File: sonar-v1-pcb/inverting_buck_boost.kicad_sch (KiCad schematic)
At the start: 0 parts

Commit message: wip
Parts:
- added U4: AP63301WU-7, Sonar:TSOT-23-6, symbol sonar_lib:AP63301WU-7
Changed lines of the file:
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@@
 	(generator_version "9.0")
 	(paper "A4")
+	(symbol
+		(lib_id "sonar_lib:AP63301WU-7")
+		(at 148.59 93.98 0)
+		(unit 1)
+		(exclude_from_sim no)
+		(in_bom yes)
+		(on_board yes)
+		(dnp no)
+		(fields_autoplaced yes)
+		(property "Reference" "U4"
+			(at 148.59 78.74 0)
+			(effects
+				(font
+					(size 1.27 1.27)
+				)
+			)
+		)
+		(property "Value" "AP63301WU-7"
+			(at 148.59 81.28 0)
+			(effects
+				(font
+					(size 1.27 1.27)
+				)
+			)
+		)
+		(property "Footprint" "Sonar:TSOT-23-6"
+			(at 148.59 63.5 0)
+			(effects
+				(font
+					(size 1.27 1.27)
+				)
+				(hide yes)
+			)
+		)
+		(property "Datasheet" "https://www.lcsc.com/datasheet/C2158003.pdf"
+			(at 148.59 76.2 0)
+			(effects
+				(font
+					(size 1.27 1.27)
+				)
+				(hide yes)
+			)
+		)
+		(property "Description" "500kHz Adjustable Buck Converter, 3A Max Current, 3.8V-32V Input Voltage"
+			(at 148.59 73.66 0)
+			(effects
+				(font
+					(size 1.27 1.27)
+				)
+				(hide yes)
+			)
+		)
+		(property "Manufacturer" "DIODES"
+			(at 148.59 58.42 0)
+			(effects
+				(font
+					(size 1.27 1.27)
+				)
+				(hide yes)
+			)
+		)
+		(property "Mfr. Part #" "AP63301WU-7"
+			(at 148.59 60.96 0)
+			(effects
+				(font
+					(size 1.27 1.27)
+				)
+				(hide yes)
+			)
+		)
+		(property "LCSC ID" "C2158003"
+			(at 148.59 71.12 0)
+			(effects
+				(font
+					(size 1.27 1.27)
+				)
+				(hide yes)
+			)
+		)
+		(property "Package" "TSOT-23-6"
+			(at 148.59 68.58 0)
+			(effects
+				(font
+					(size 1.27 1.27)
+				)
+				(hide yes)
+			)
+		)
+		(property "Spice Warning Override" "No SPICE model available"
+			(at 148.59 66.04 0)
+			(effects
+				(font
+					(size 1.27 1.27)
+				)
+				(hide yes)
+			)
+		)
+		(pin "4"
+		)
+		(pin "2"
+		)
+		(pin "1"
+		)
+		(pin "5"
+		)
+		(pin "6"
+		)
+		(pin "3"
+		)
+		(instances
+			(project ""
+				(path "/f72ceae0-eee4-4385-b0e8-639846bcb5f2/0971c334-b681-41ae-ad35-a89520df0687/b540816d-de86-42bd-acdb-d7039b5ee686"
+					(reference "U4")
+					(unit 1)
+				)
+			)
+		)
+	)
 )

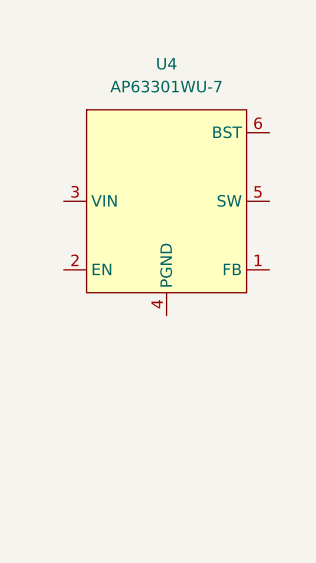
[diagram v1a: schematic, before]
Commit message: Add a buck converter for the inverting buck boost
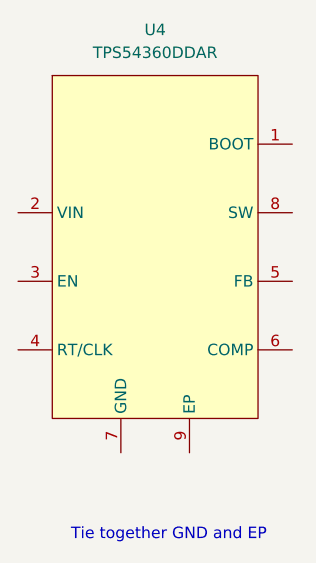
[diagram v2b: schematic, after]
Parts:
- removed U4: AP63301WU-7, Sonar:TSOT-23-6, symbol sonar_lib:AP63301WU-7
- added U4: TPS54360DDAR, GS_SO:SOIC-8-1EP_3.9x4.9mm_P1.27mm_EP2.29x3mm, symbol GS_Switching_Regulators:TPS54360DDAR
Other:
- note added: "Tie together GND and EP"
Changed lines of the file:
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@@
 	(generator_version "9.0")
 	(paper "A4")
+	(text "Tie together GND and EP"
+		(exclude_from_sim no)
+		(at 148.844 131.064 0)
+		(effects
+			(font
+				(size 1.27 1.27)
+			)
+		)
+	)
 	(symbol
-		(lib_id "sonar_lib:AP63301WU-7")
-		(at 148.59 93.98 0)
+		(lib_id "GS_Switching_Regulators:TPS54360DDAR")
+		(at 147.32 99.06 0)
 		(unit 1)
 		(exclude_from_sim no)
@@
 		(fields_autoplaced yes)
 		(property "Reference" "U4"
-			(at 148.59 78.74 0)
+			(at 147.32 74.93 0)
 			(effects
 				(font
@@
 			)
 		)
-		(property "Value" "AP63301WU-7"
-			(at 148.59 81.28 0)
+		(property "Value" "TPS54360DDAR"
+			(at 147.32 77.47 0)
 			(effects
 				(font
@@
 			)
 		)
-		(property "Footprint" "Sonar:TSOT-23-6"
-			(at 148.59 63.5 0)
+		(property "Footprint" "GS_SO:SOIC-8-1EP_3.9x4.9mm_P1.27mm_EP2.29x3mm"
+			(at 147.32 66.04 0)
 			(effects
 				(font
@@
 			)
 		)
-		(property "Datasheet" "https://www.lcsc.com/datasheet/C2158003.pdf"
-			(at 148.59 76.2 0)
+		(property "Datasheet" "https://www.lcsc.com/datasheet/C44377.pdf"
+			(at 147.32 58.42 0)
 			(effects
 				(font
@@
 			)
 		)
-		(property "Description" "500kHz Adjustable Buck Converter, 3A Max Current, 3.8V-32V Input Voltage"
-			(at 148.59 73.66 0)
+		(property "Description" "2.5MHz Adjustable Buck Converter, 4.5V-60V Input Voltage, 3.5A Max Current"
+			(at 147.32 68.58 0)
 			(effects
 				(font
@@
 			)
 		)
-		(property "Manufacturer" "DIODES"
-			(at 148.59 58.42 0)
+		(property "Manufacturer" "TI"
+			(at 147.32 73.66 0)
 			(effects
 				(font
@@
 			)
 		)
-		(property "Mfr. Part #" "AP63301WU-7"
-			(at 148.59 60.96 0)
+		(property "Mfr. Part #" "TPS54360DDAR"
+			(at 147.32 60.96 0)
 			(effects
 				(font
@@
 			)
 		)
-		(property "LCSC ID" "C2158003"
-			(at 148.59 71.12 0)
+		(property "LCSC ID" "C44377"
+			(at 147.32 63.5 0)
 			(effects
 				(font
@@
 			)
 		)
-		(property "Package" "TSOT-23-6"
-			(at 148.59 68.58 0)
+		(property "Package" "SOIC-8-EP"
+			(at 147.32 71.12 0)
 			(effects
 				(font
@@
 			)
 		)
-		(property "Spice Warning Override" "No SPICE model available"
-			(at 148.59 66.04 0)
-			(effects
-				(font
-					(size 1.27 1.27)
-				)
-				(hide yes)
-			)
+		(pin "5"
 		)
 		(pin "4"
 		)
-		(pin "2"
+		(pin "7"
+		)
+		(pin "9"
+		)
+		(pin "3"
+		)
+		(pin "8"
 		)
 		(pin "1"
 		)
-		(pin "5"
+		(pin "2"
 		)
 		(pin "6"
 		)
-		(pin "3"
-		)
 		(instances

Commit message: formatting lol
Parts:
- removed U4: TPS54360DDAR, GS_SO:SOIC-8-1EP_3.9x4.9mm_P1.27mm_EP2.29x3mm, symbol GS_Switching_Regulators:TPS54360DDAR
- added U4: AP63301WU-7, Sonar:TSOT-23-6, symbol sonar_lib:AP63301WU-7
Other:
- note removed: "Tie together GND and EP"
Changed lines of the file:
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@@
 	(generator_version "9.0")
 	(paper "A4")
-	(text "Tie together GND and EP"
-		(exclude_from_sim no)
-		(at 148.844 131.064 0)
-		(effects
-			(font
-				(size 1.27 1.27)
-			)
-		)
-	)
 	(symbol
-		(lib_id "GS_Switching_Regulators:TPS54360DDAR")
-		(at 147.32 99.06 0)
+		(lib_id "sonar_lib:AP63301WU-7")
+		(at 148.59 93.98 0)
 		(unit 1)
 		(exclude_from_sim no)
@@
 		(fields_autoplaced yes)
 		(property "Reference" "U4"
-			(at 147.32 74.93 0)
+			(at 148.59 78.74 0)
 			(effects
 				(font
@@
 			)
 		)
-		(property "Value" "TPS54360DDAR"
-			(at 147.32 77.47 0)
+		(property "Value" "AP63301WU-7"
+			(at 148.59 81.28 0)
 			(effects
 				(font
@@
 			)
 		)
-		(property "Footprint" "GS_SO:SOIC-8-1EP_3.9x4.9mm_P1.27mm_EP2.29x3mm"
-			(at 147.32 66.04 0)
+		(property "Footprint" "Sonar:TSOT-23-6"
+			(at 148.59 63.5 0)
 			(effects
 				(font
@@
 			)
 		)
-		(property "Datasheet" "https://www.lcsc.com/datasheet/C44377.pdf"
-			(at 147.32 58.42 0)
+		(property "Datasheet" "https://www.lcsc.com/datasheet/C2158003.pdf"
+			(at 148.59 76.2 0)
 			(effects
 				(font
@@
 			)
 		)
-		(property "Description" "2.5MHz Adjustable Buck Converter, 4.5V-60V Input Voltage, 3.5A Max Current"
-			(at 147.32 68.58 0)
+		(property "Description" "500kHz Adjustable Buck Converter, 3A Max Current, 3.8V-32V Input Voltage"
+			(at 148.59 73.66 0)
 			(effects
 				(font
@@
 			)
 		)
-		(property "Manufacturer" "TI"
-			(at 147.32 73.66 0)
+		(property "Manufacturer" "DIODES"
+			(at 148.59 58.42 0)
 			(effects
 				(font
@@
 			)
 		)
-		(property "Mfr. Part #" "TPS54360DDAR"
-			(at 147.32 60.96 0)
+		(property "Mfr. Part #" "AP63301WU-7"
+			(at 148.59 60.96 0)
 			(effects
 				(font
@@
 			)
 		)
-		(property "LCSC ID" "C44377"
-			(at 147.32 63.5 0)
+		(property "LCSC ID" "C2158003"
+			(at 148.59 71.12 0)
 			(effects
 				(font
@@
 			)
 		)
-		(property "Package" "SOIC-8-EP"
-			(at 147.32 71.12 0)
+		(property "Package" "TSOT-23-6"
+			(at 148.59 68.58 0)
 			(effects
 				(font
@@
 			)
 		)
-		(pin "5"
+		(property "Spice Warning Override" "No SPICE model available"
+			(at 148.59 66.04 0)
+			(effects
+				(font
+					(size 1.27 1.27)
+				)
+				(hide yes)
+			)
 		)
 		(pin "4"
 		)
-		(pin "7"
+		(pin "2"
 		)
-		(pin "9"
+		(pin "1"
+		)
+		(pin "5"
+		)
+		(pin "6"
 		)
 		(pin "3"
 		)
-		(pin "8"
-		)
-		(pin "1"
-		)
-		(pin "2"
-		)
-		(pin "6"
-		)
 		(instances

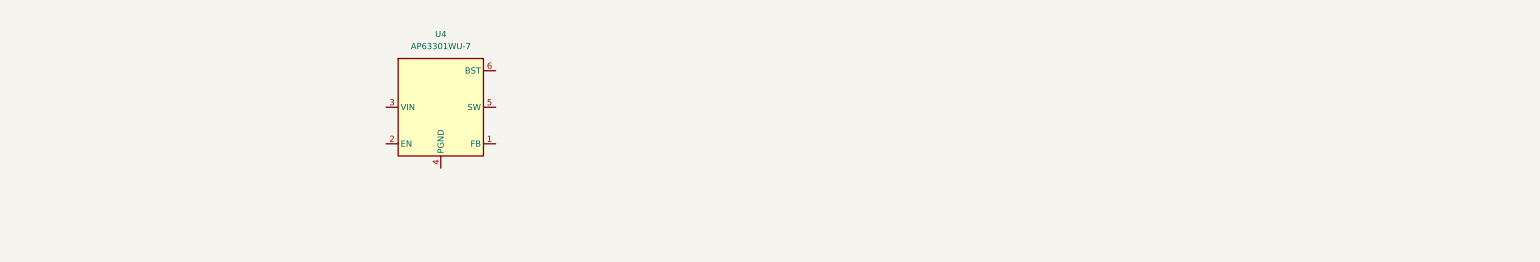
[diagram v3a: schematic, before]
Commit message: Update inverting buck boost schematic
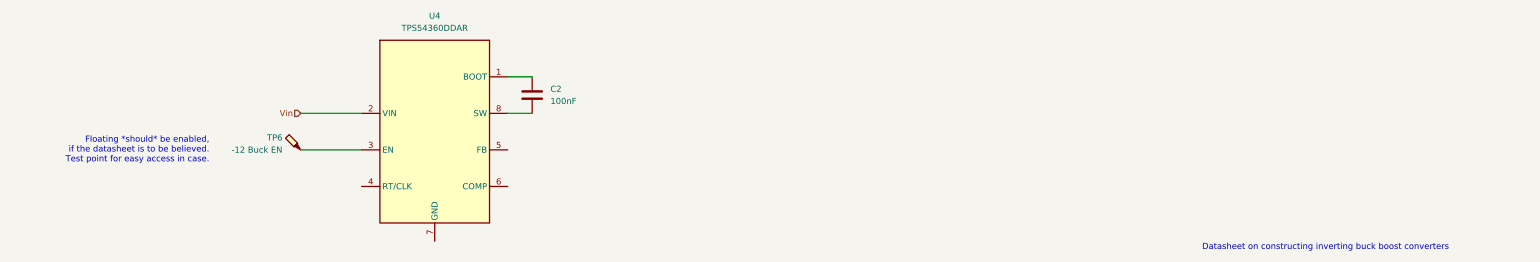
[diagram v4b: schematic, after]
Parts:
- removed U4: AP63301WU-7, Sonar:TSOT-23-6, symbol sonar_lib:AP63301WU-7
- added C2: 100nF, Sonar:C_0603_1608Metric, symbol sonar_lib:C_0603_100nF
- added TP6: -12 Buck EN, symbol Connector:TestPoint_Probe
- added U4: TPS54360DDAR, GS_SO:SOIC-8-1EP_3.9x4.9mm_P1.27mm_EP2.29x3mm, symbol GS_Switching_Regulators:TPS54360DDAR
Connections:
- new net: TP6.1, U4.3 (EN)
- new net: C2.1, U4.1 (BOOT)
- new net: C2.2, U4.8 (SW)
- new net: U4.7 (GND), U4.9 (GND)
- new net Vin: U4.2 (VIN)
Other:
- note added: "Datasheet on constructing inverting buck boost converters"
- note added: "Floating *should* be enabled, if the datasheet is to be believed. Test point for easy access in case."
- title: (none) -> -12V Inverting Buck Boost

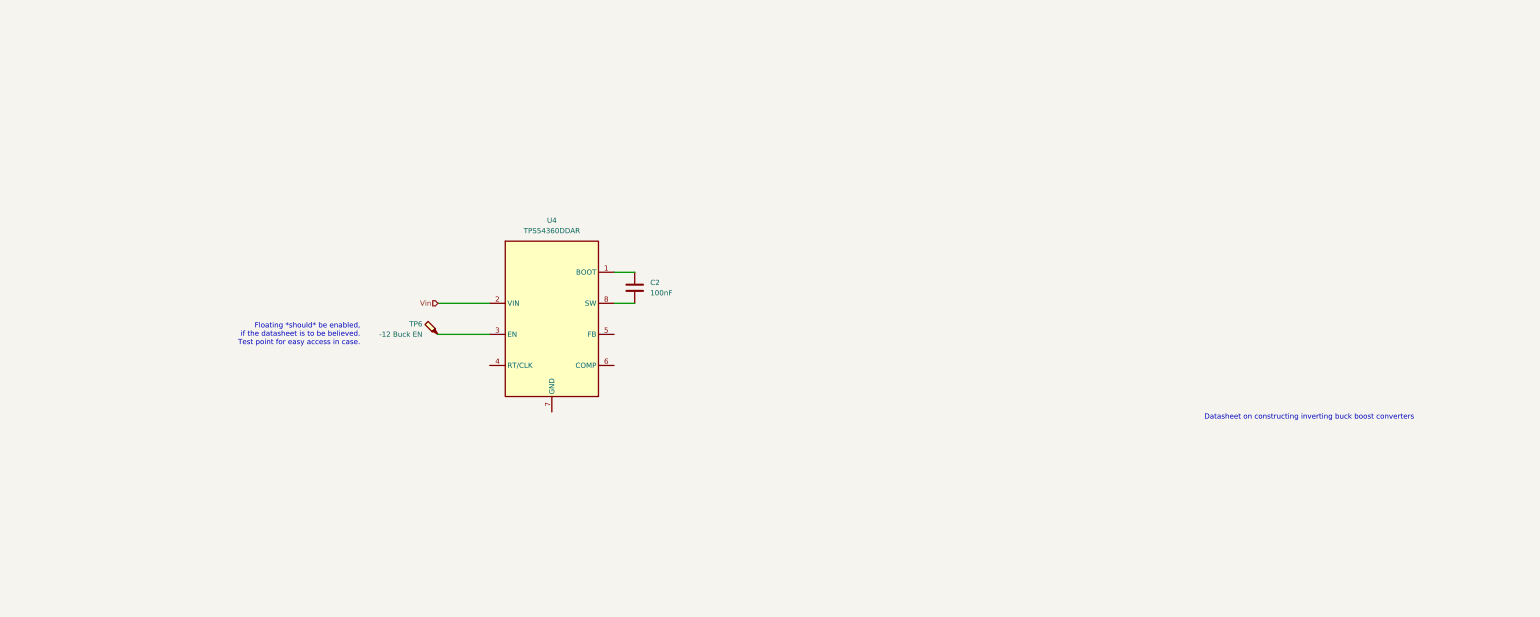
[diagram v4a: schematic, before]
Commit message: Do some more questionable math for the inverting buck boost
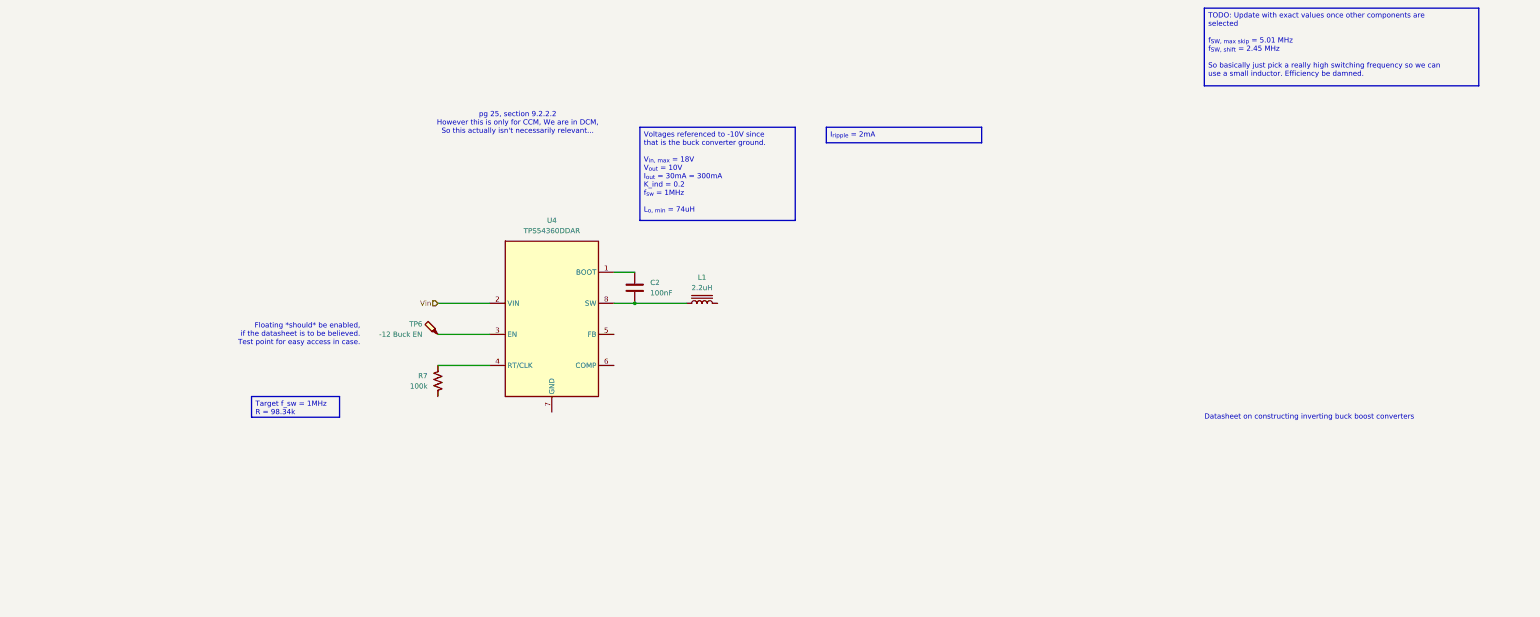
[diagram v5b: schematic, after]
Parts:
- added L1: 2.2uH, Sonar:L_1008_2520Metric, symbol sonar_lib:L_1008_2.2uH
- added R7: 100k, Sonar:R_0603_1608Metric, symbol sonar_lib:R_0603_100k
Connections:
- net at C2.2, U4.8 (SW): now also L1.1
- net at U4.4 (RT/CLK): now also R7.1
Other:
- note added: "pg 25, section 9.2.2.2 However this is only for CCM, We are in DCM, So this actually isn't necessarily relevant..."

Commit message: Finish -12V buck
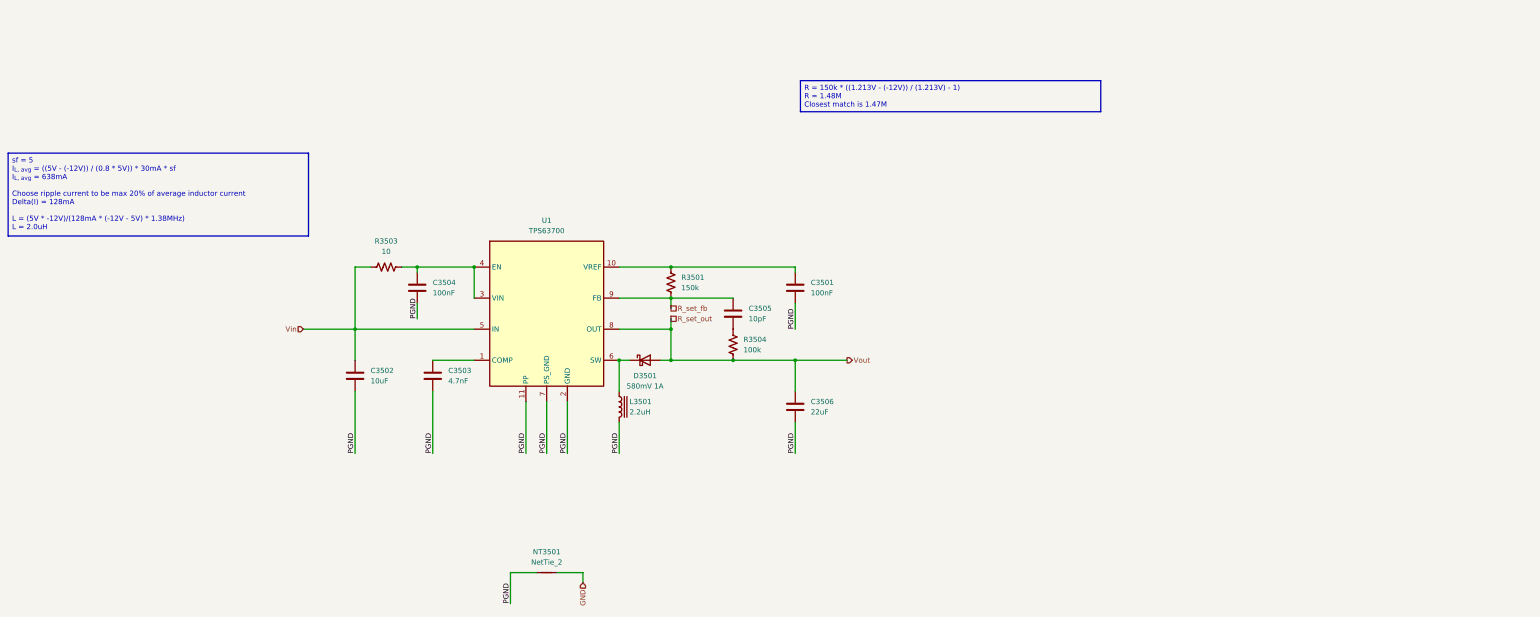
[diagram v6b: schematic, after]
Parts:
- removed C2: 100nF, Sonar:C_0603_1608Metric, symbol sonar_lib:C_0603_100nF
- removed L1: 2.2uH, Sonar:L_1008_2520Metric, symbol sonar_lib:L_1008_2.2uH
- removed R7: 100k, Sonar:R_0603_1608Metric, symbol sonar_lib:R_0603_100k
- removed TP6: -12 Buck EN, symbol Connector:TestPoint_Probe
- removed U4: TPS54360DDAR, GS_SO:SOIC-8-1EP_3.9x4.9mm_P1.27mm_EP2.29x3mm, symbol GS_Switching_Regulators:TPS54360DDAR
- added C3501: 100nF, Sonar:C_0603_1608Metric, symbol sonar_lib:C_0603_22uF
- added C3502: 10uF, Sonar:C_0603_1608Metric, symbol sonar_lib:C_0603_10uF
- added C3503: 4.7nF, Sonar:C_0603_1608Metric, symbol sonar_lib:C_0603_4.7nF
- added C3504: 100nF, Sonar:C_0603_1608Metric, symbol sonar_lib:C_0603_100nF
- added C3505: 10pF, Sonar:C_0603_1608Metric, symbol sonar_lib:C_0603_10pF
- added C3506: 22uF, Sonar:C_0603_1608Metric, symbol sonar_lib:C_0603_22uF
- added D3501: 580mV 1A, Sonar:D_SOD-123, symbol sonar_lib:D_Schottky_580mV_1A
- added L3501: 2.2uH, Sonar:L_1008_2520Metric, symbol sonar_lib:L_1008_2.2uH
- added NT3501: NetTie_2, symbol sonar_lib:NetTie_2
- added R3501: 150k, Sonar:R_0603_1608Metric, symbol sonar_lib:R_0603_150k
- added R3503: 10, Sonar:R_0603_1608Metric, symbol sonar_lib:R_0603_10
- added R3504: 100k, Sonar:R_0603_1608Metric, symbol sonar_lib:R_0603_100k
- added U1: TPS63700, Sonar:VSON-10_L3.0-W3.0-P0.50-TL-EP, symbol sonar_lib:TPS63700
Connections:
- net Vin: now also C3502.1, R3503.1, U1.5 (IN)
- new net: D3501.1 (K), L3501.1, U1.6 (SW)
- new net: C3505.2, R3504.1
- new net: C3501.1, R3501.1, U1.10 (VREF)
- new net: C3503.1, U1.1 (COMP)
- new net: C3504.1, R3503.2, U1.3 (VIN), U1.4 (EN)
- new net GND: NT3501.2
- new net PGND: C3501.2, C3502.2, C3503.2, C3504.2, C3506.2, L3501.2, NT3501.1, U1.11 (PP), U1.2 (GND), U1.7 (PS_GND)
- new net R_set_fb: C3505.1, R3501.2, U1.9 (FB)
- new net R_set_out: C3506.1, D3501.2 (A), R3504.2, U1.8 (OUT)
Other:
- note removed: "Datasheet on constructing inverting buck boost converters"
- note removed: "Floating *should* be enabled, if the datasheet is to be believed. Test point for easy access in case."
- note removed: "pg 25, section 9.2.2.2 However this is only for CCM, We are in DCM, So this actually isn't necessarily relevant..."
- title: -12V Inverting Buck Boost -> Adjustable Inverting Buck Boost
